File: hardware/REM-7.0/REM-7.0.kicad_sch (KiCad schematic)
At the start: 22 parts, among them J1 Conn_01x04, J2 Conn_01x05, Q1 MMBT3904, T1 Transformer_1P_1S

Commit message: modified:   CHANGELOG.md 	modified:   archive/REM - Vsense.xlsx 	modified:   archive/REM_OUTPUT.xlsx 	modified:   hardware/REM-7.0/REM-7.0.kicad_pcb 	modified:   hardware/REM-7.0/REM-7.0.kicad_prl 	modified:   hardware/REM-7.0/REM-7.0.kicad_pro 	modified:   hardware/REM-7.0/REM-7.0.kicad_sch 	modified:   hardware/REM-7.0/REM-7.op.raw 	modified:   hardware/REM-7.0/REM-7.raw 	new file:   hardware/REM-7.0/pabrication output/REM-7.0-B_Cu.dxf 	modified:   hardware/REM-7.0/pabrication output/REM-7.0-B_Cu.pdf 	new file:   hardware/REM-7.0/pabrication output/REM-7.0-Edge_Cuts.dxf 	modified:   hardware/REM-7.0/pabrication output/REM-7.0-Edge_Cuts.pdf 	new file:   hardware/REM-7.0/pabrication output/REM-7.0-F_Cu.dxf 	modified:   hardware/REM-7.0/pabrication output/REM-7.0-F_Cu.pdf 	modified:   hardware/REM-7.0/pabrication output/TRACE_BOT.dxf 	new file:   hardware/REM-7.0/pabrication output/TRACE_TOP.dxf.dwg
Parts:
- added RV_ALT1: R, Resistor_SMD:R_0805_2012Metric_Pad1.20x1.40mm_HandSolder, symbol Device:R
- R3: value R -> 4.7k
- T1: footprint (none) -> Transformer_THT:Transformer_EP13_1423
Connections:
- net GND: now also RV_ALT1.2
- net REM: now also RV_ALT1.1
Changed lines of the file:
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@@
 	)
 	(junction
+		(at 76.2 50.8)
+		(diameter 0)
+		(color 0 0 0 0)
+	)
+	(junction
 		(at 177.8 50.8)
 		(diameter 0)
@@
 	)
 	(junction
-		(at 76.2 50.8)
+		(at 165.1 63.5)
 		(diameter 0)
 		(color 0 0 0 0)
 	)
 	(junction
-		(at 165.1 63.5)
+		(at 58.42 133.35)
 		(diameter 0)
 		(color 0 0 0 0)
 	)
 	(junction
-		(at 58.42 133.35)
+		(at 213.36 48.26)
 		(diameter 0)
 		(color 0 0 0 0)
 	)
 	(junction
-		(at 213.36 48.26)
+		(at 63.5 50.8)
 		(diameter 0)
 		(color 0 0 0 0)
@@
 	)
 	(junction
+		(at 76.2 63.5)
+		(diameter 0)
+		(color 0 0 0 0)
+	)
+	(junction
 		(at 101.6 63.5)
 		(diameter 0)
@@
 	(wire
 		(pts
+			(xy 63.5 60.96) (xy 63.5 63.5)
+		)
+		(stroke
+			(width 0)
+			(type default)
+		)
+	)
+	(wire
+		(pts
+			(xy 63.5 63.5) (xy 76.2 63.5)
+		)
+		(stroke
+			(width 0)
+			(type default)
+		)
+	)
+	(wire
+		(pts
 			(xy 165.1 60.96) (xy 165.1 63.5)
 		)
@@
 	(wire
 		(pts
+			(xy 63.5 50.8) (xy 76.2 50.8)
+		)
+		(stroke
+			(width 0)
+			(type default)
+		)
+	)
+	(wire
+		(pts
 			(xy 139.7 57.15) (xy 139.7 66.04)
 		)
@@
 	(wire
 		(pts
+			(xy 63.5 50.8) (xy 63.5 53.34)
+		)
+		(stroke
+			(width 0)
+			(type default)
+		)
+	)
+	(wire
+		(pts
 			(xy 226.06 45.72) (xy 213.36 45.72)
 		)
@@
 	(wire
 		(pts
-			(xy 63.5 50.8) (xy 76.2 50.8)
+			(xy 50.8 50.8) (xy 63.5 50.8)
 		)
 		(stroke
@@
 	)
 	(label "REM"
-		(at 66.04 50.8 0)
+		(at 53.34 50.8 0)
 		(effects
 			(font
@@
 			(effects
 				(font
-					(size 1.27 1.27)
+					(size 1 1)
 				)
 				(justify left)
@@
 			(effects
 				(font
-					(size 1 1)
+					(size 1.27 1.27)
 				)
 				(justify left)
@@
 			(effects
 				(font
-					(size 1.27 1.27)
+					(size 1 1)
 				)
 				(justify left)
@@
 			(effects
 				(font
-					(size 1.27 1.27)
+					(size 1 1)
 				)
 				(justify right)
@@
 			(effects
 				(font
-					(size 1.27 1.27)
+					(size 1 1)
 				)
 				(justify left)
@@
 			(effects
 				(font
-					(size 1.27 1.27)
+					(size 1 1)
 				)
 				(justify left)
@@
 		(dnp no)
 		(property "Reference" "R7"
-			(at 194.31 45.974 90)
+			(at 194.31 45.72 90)
 			(show_name no)
 			(do_not_autoplace no)
 			(effects
 				(font
-					(size 1 1)
+					(size 1.27 1.27)
 				)
 			)
 		)
 		(property "Value" "33R 2W"
-			(at 194.31 50.546 90)
+			(at 194.31 50.8 90)
 			(show_name no)
 			(do_not_autoplace no)
@@
 			)
 		)
-		(property "Footprint" ""
+		(property "Footprint" "Transformer_THT:Transformer_EP13_1423"
 			(at 184.15 44.45 0)
 			(hide yes)
@@
 		(dnp no)
 		(property "Reference" "R6"
-			(at 194.31 38.354 90)
+			(at 194.31 38.1 90)
 			(show_name no)
 			(do_not_autoplace no)
 			(effects
 				(font
-					(size 1 1)
+					(size 1.27 1.27)
 				)
 			)
 		)
 		(property "Value" "33R 2W"
-			(at 194.31 42.926 90)
+			(at 194.31 43.18 90)
 			(show_name no)
 			(do_not_autoplace no)
@@
 			(effects
 				(font
-					(size 1.27 1.27)
+					(size 1 1)
 				)
 				(justify left)
@@
 			(effects
 				(font
-					(size 1 1)
+					(size 1.27 1.27)
 				)
 				(justify left)
@@
 			(effects
 				(font
-					(size 1.27 1.27)
+					(size 1 1)
 				)
 				(justify left)
@@
 			(effects
 				(font
-					(size 1.27 1.27)
+					(size 1 1)
 				)
 				(justify right)
@@
 			(effects
 				(font
-					(size 1.27 1.27)
+					(size 1 1)
 				)
 				(justify left)
@@
 			(effects
 				(font
-					(size 1.27 1.27)
+					(size 1 1)
 				)
 				(justify left)
@@
 		(dnp no)
 		(property "Reference" "R3"
-			(at 95.25 44.45 90)
+			(at 95.25 48.26 90)
 			(show_name no)
 			(do_not_autoplace no)
@@
 			)
 		)
-		(property "Value" "R"
-			(at 95.25 46.99 90)
+		(property "Value" "4.7k"
+			(at 95.25 53.34 90)
 			(show_name no)
 			(do_not_autoplace no)
 			(effects
 				(font
-					(size 1.27 1.27)
+					(size 1 1)
 				)
 			)
@@
 	)
 	(symbol
+		(lib_id "Device:R")
+		(at 63.5 57.15 0)
+		(mirror y)
+		(unit 1)
+		(body_style 1)
+		(exclude_from_sim no)
+		(in_bom yes)
+		(on_board yes)
+		(in_pos_files yes)
+		(dnp no)
+		(property "Reference" "RV_ALT1"
+			(at 60.96 55.88 0)
+			(show_name no)
+			(do_not_autoplace no)
+			(effects
+				(font
+					(size 1.27 1.27)
+				)
+				(justify left)
+			)
+		)
+		(property "Value" "R"
+			(at 60.96 58.42 0)
+			(show_name no)
+			(do_not_autoplace no)
+			(effects
+				(font
+					(size 1 1)
+				)
+				(justify left)
+			)
+		)
+		(property "Footprint" "Resistor_SMD:R_0805_2012Metric_Pad1.20x1.40mm_HandSolder"
+			(at 65.278 57.15 90)
+			(hide yes)
+			(show_name no)
+			(do_not_autoplace no)
+			(effects
+				(font
+					(size 1.27 1.27)
+				)
+			)
+		)
+		(property "Datasheet" ""
+			(at 63.5 57.15 0)
+			(hide yes)
+			(show_name no)
+			(do_not_autoplace no)
+			(effects
+				(font
+					(size 1.27 1.27)
+				)
+			)
+		)
+		(property "Description" "Resistor"
+			(at 63.5 57.15 0)
+			(hide yes)
+			(show_name no)
+			(do_not_autoplace no)
+			(effects
+				(font
+					(size 1.27 1.27)
+				)
+			)
+		)
+		(pin "2"
+		)
+		(pin "1"
+		)
+		(instances
+			(project "REM-7.0"
+				(path "/17c3600d-8355-46a2-9621-93cd471aba8c"
+					(reference "RV_ALT1")
+					(unit 1)
+				)
+			)
+		)
+	)
+	(symbol
 		(lib_id "Connector_Generic:Conn_01x05")
 		(at 231.14 45.72 0)
@@
 		(dnp no)
 		(property "Reference" "C6"
-			(at 133.35 44.45 90)
+			(at 133.35 46.99 90)
 			(show_name no)
 			(do_not_autoplace no)
@@
 		)
 		(property "Value" "10n"
-			(at 133.35 46.99 90)
+			(at 133.35 54.61 90)
 			(show_name no)
 			(do_not_autoplace no)
 			(effects
 				(font
-					(size 1.27 1.27)
+					(size 1 1)
 				)
 			)

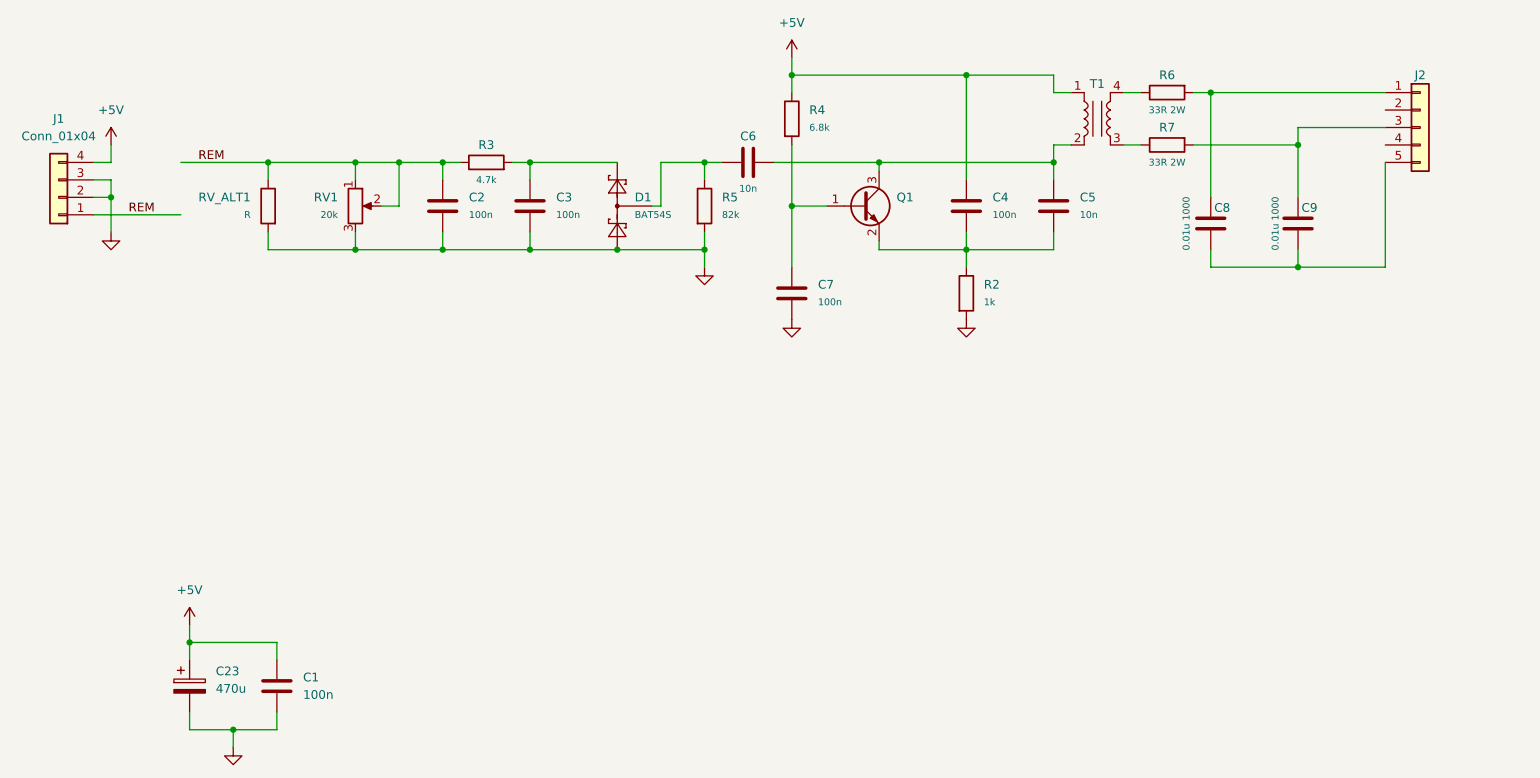
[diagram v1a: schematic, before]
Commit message: modified:   hardware/REM-7.0/REM-7.0.kicad_pro 	modified:   hardware/REM-7.0/REM-7.0.kicad_sch 	renamed:    hardware/REM-7.0/pabrication output/EDGE.dxf -> hardware/REM-7.0/fabrication output/EDGE.dxf 	renamed:    hardware/REM-7.0/pabrication output/REM-7.0-B_Cu.dxf -> hardware/REM-7.0/fabrication output/REM-7.0-B_Cu.dxf 	renamed:    hardware/REM-7.0/pabrication output/REM-7.0-B_Cu.pdf -> hardware/REM-7.0/fabrication output/REM-7.0-B_Cu.pdf 	renamed:    hardware/REM-7.0/pabrication output/REM-7.0-Edge_Cuts.dxf -> hardware/REM-7.0/fabrication output/REM-7.0-Edge_Cuts.dxf 	renamed:    hardware/REM-7.0/pabrication output/REM-7.0-Edge_Cuts.pdf -> hardware/REM-7.0/fabrication output/REM-7.0-Edge_Cuts.pdf 	renamed:    hardware/REM-7.0/pabrication output/REM-7.0-F_Cu.dxf -> hardware/REM-7.0/fabrication output/REM-7.0-F_Cu.dxf 	renamed:    hardware/REM-7.0/pabrication output/REM-7.0-F_Cu.pdf -> hardware/REM-7.0/fabrication output/REM-7.0-F_Cu.pdf 	renamed:    hardware/REM-7.0/pabrication output/TRACE_BOT.dxf -> hardware/REM-7.0/fabrication output/TRACE_BOT.dxf 	renamed:    hardware/REM-7.0/pabrication output/TRACE_TOP.dxf -> hardware/REM-7.0/fabrication output/TRACE_TOP.dxf
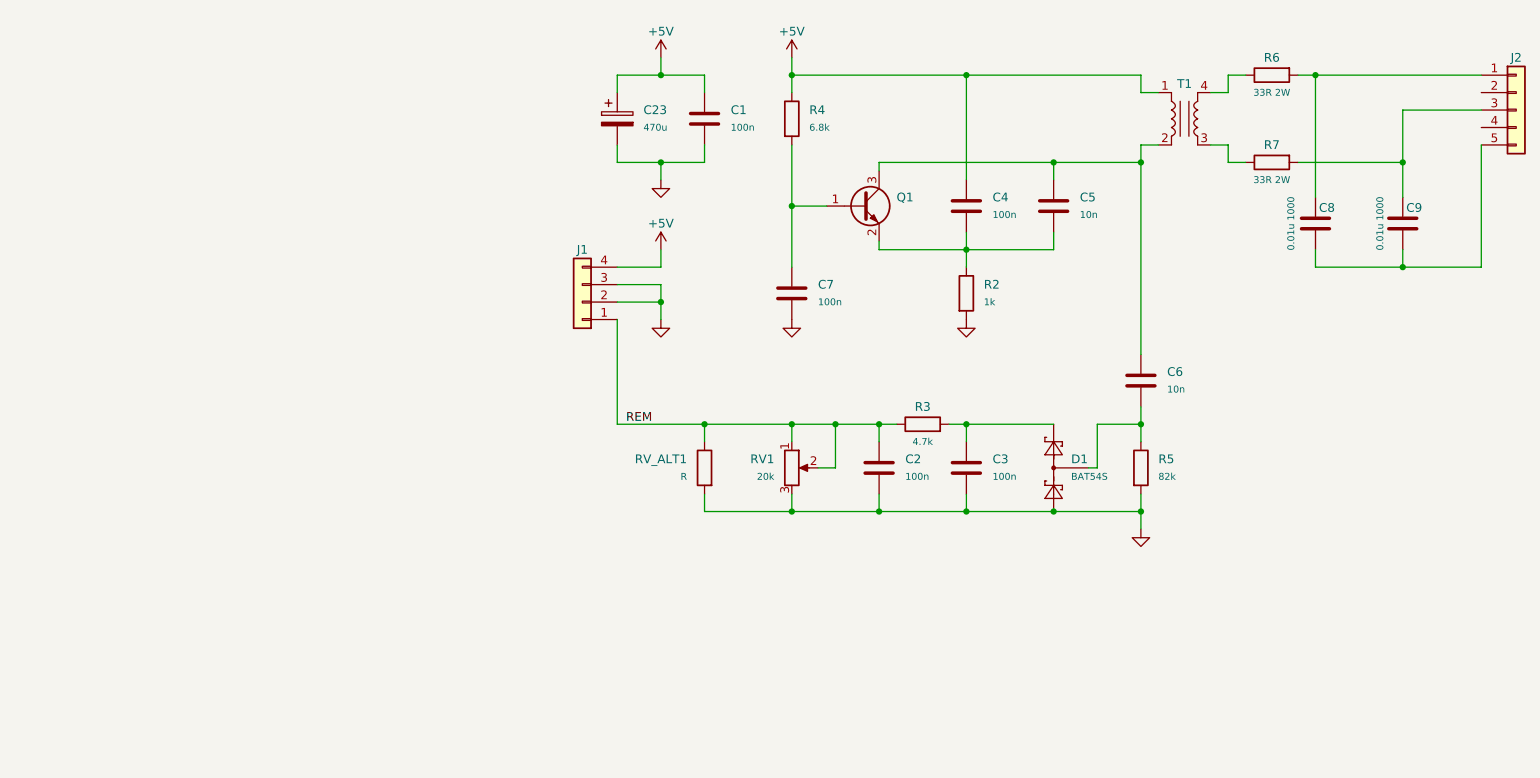
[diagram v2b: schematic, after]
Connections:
- net at C5.1, Q1.3 (C), T1.2 (AB): now also C6.1; no longer C6.2
- net at D1.3 (COM), R5.1: now also C6.2; no longer C6.1
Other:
- moved on the sheet: C1, C2, C23, C3, C8, C9, D1, J1, J2, R3, R5, R6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

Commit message: new file:   archive/Peripheral Migration ESP32S3-STM32H7.md 	new file:   archive/datasheets/STM32H750VBT6_STM32H7XX_M-2.jpg 	new file:   archive/datasheets/original-schematic-STM32H7XX-M.pdf 	new file:   archive/datasheets/stm32h750ib.pdf 	new file:   hardware/CTL-7.0/CTL-7.0.kicad_pcb 	new file:   hardware/CTL-7.0/CTL-7.0.kicad_prl 	new file:   hardware/CTL-7.0/CTL-7.0.kicad_pro 	new file:   hardware/CTL-7.0/CTL-7.0.kicad_sch 	modified:   hardware/REM-7.0/REM-7.0.kicad_pcb 	modified:   hardware/REM-7.0/REM-7.0.kicad_prl 	modified:   hardware/REM-7.0/REM-7.0.kicad_pro 	modified:   hardware/REM-7.0/REM-7.0.kicad_sch
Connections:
- net GND: now also RV1.1, RV1.2; no longer RV1.3
- net REM: now also RV1.3; no longer RV1.1, RV1.2
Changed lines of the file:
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@@
+	)
+	(junction
+		(at 146.05 101.6)
+		(diameter 0)
+		(color 0 0 0 0)
 	)
 	(junction
@@
 	)
 	(junction
-		(at 146.05 88.9)
-		(diameter 0)
-		(color 0 0 0 0)
-	)
-	(junction
 		(at 152.4 101.6)
 		(diameter 0)
@@
 	(wire
 		(pts
-			(xy 139.7 88.9) (xy 146.05 88.9)
+			(xy 139.7 88.9) (xy 152.4 88.9)
 		)
 		(stroke
@@
 	(wire
 		(pts
+			(xy 139.7 101.6) (xy 146.05 101.6)
+		)
+		(stroke
+			(width 0)
+			(type default)
+		)
+	)
+	(wire
+		(pts
 			(xy 139.7 35.56) (xy 139.7 38.1)
 		)
@@
 	(wire
 		(pts
+			(xy 146.05 101.6) (xy 152.4 101.6)
+		)
+		(stroke
+			(width 0)
+			(type default)
+		)
+	)
+	(wire
+		(pts
 			(xy 165.1 60.96) (xy 165.1 63.5)
 		)
@@
 	(wire
 		(pts
-			(xy 146.05 88.9) (xy 152.4 88.9)
-		)
-		(stroke
-			(width 0)
-			(type default)
-		)
-	)
-	(wire
-		(pts
 			(xy 139.7 48.26) (xy 139.7 57.15)
 		)
@@
 	(wire
 		(pts
-			(xy 146.05 95.25) (xy 146.05 88.9)
-		)
-		(stroke
-			(width 0)
-			(type default)
-		)
-	)
-	(wire
-		(pts
 			(xy 177.8 50.8) (xy 190.5 50.8)
 		)
@@
 	(wire
 		(pts
+			(xy 146.05 95.25) (xy 146.05 101.6)
+		)
+		(stroke
+			(width 0)
+			(type default)
+		)
+	)
+	(wire
+		(pts
 			(xy 215.9 63.5) (xy 215.9 66.04)
 		)
@@
 	(wire
 		(pts
-			(xy 139.7 101.6) (xy 152.4 101.6)
-		)
-		(stroke
-			(width 0)
-			(type default)
-		)
-	)
-	(wire
-		(pts
 			(xy 228.6 50.8) (xy 228.6 55.88)
 		)
@@
 	(wire
 		(pts
+			(xy 143.51 95.25) (xy 146.05 95.25)
+		)
+		(stroke
+			(width 0)
+			(type default)
+		)
+	)
+	(wire
+		(pts
 			(xy 114.3 71.12) (xy 120.65 71.12)
 		)
@@
 		(pts
 			(xy 165.1 101.6) (xy 177.8 101.6)
-		)
-		(stroke
-			(width 0)
-			(type default)
-		)
-	)
-	(wire
-		(pts
-			(xy 143.51 95.25) (xy 146.05 95.25)
 		)
 		(stroke
@@
 		(lib_id "Device:R_Potentiometer")
 		(at 139.7 95.25 0)
+		(mirror x)
 		(unit 1)
 		(body_style 1)
@@
 		(in_pos_files yes)
 		(dnp no)
-		(fields_autoplaced yes)
 		(property "Reference" "RV1"
+			(at 137.16 96.52 0)
+			(show_name no)
+			(do_not_autoplace no)
+			(effects
+				(font
+					(size 1.27 1.27)
+				)
+				(justify right)
+			)
+		)
+		(property "Value" "20k"
 			(at 137.16 93.98 0)
 			(show_name no)
 			(do_not_autoplace no)
-			(effects
-				(font
-					(size 1.27 1.27)
-				)
-				(justify right)
-			)
-		)
-		(property "Value" "20k"
-			(at 137.16 96.52 0)
-			(show_name no)
-			(do_not_autoplace no)
